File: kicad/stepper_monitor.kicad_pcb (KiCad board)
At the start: 2 copper layers, 44 x 48 mm, 89 parts, among them J1 Conn_01x02_Pin, J2 Conn_01x04_Pin, J3 USB_C_Receptacle_USB2.0, J4 Conn_01x04_Pin, J5 Conn_01x04_Pin, J6 JTAG, Q1 MMDT2222A, SW1 SW_Push, U1 5V, U2 AMS1117-3.3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

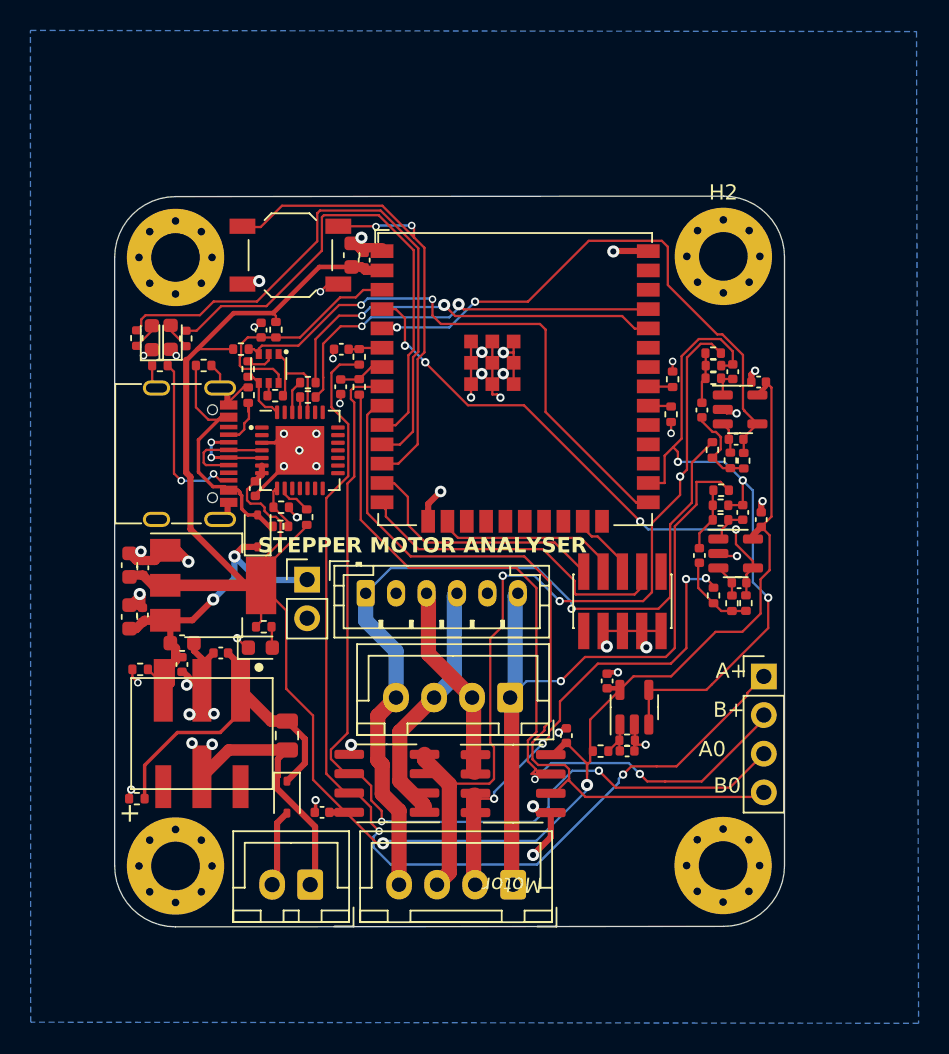
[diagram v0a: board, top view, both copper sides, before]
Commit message: Used ESP32 with Integrated antenna
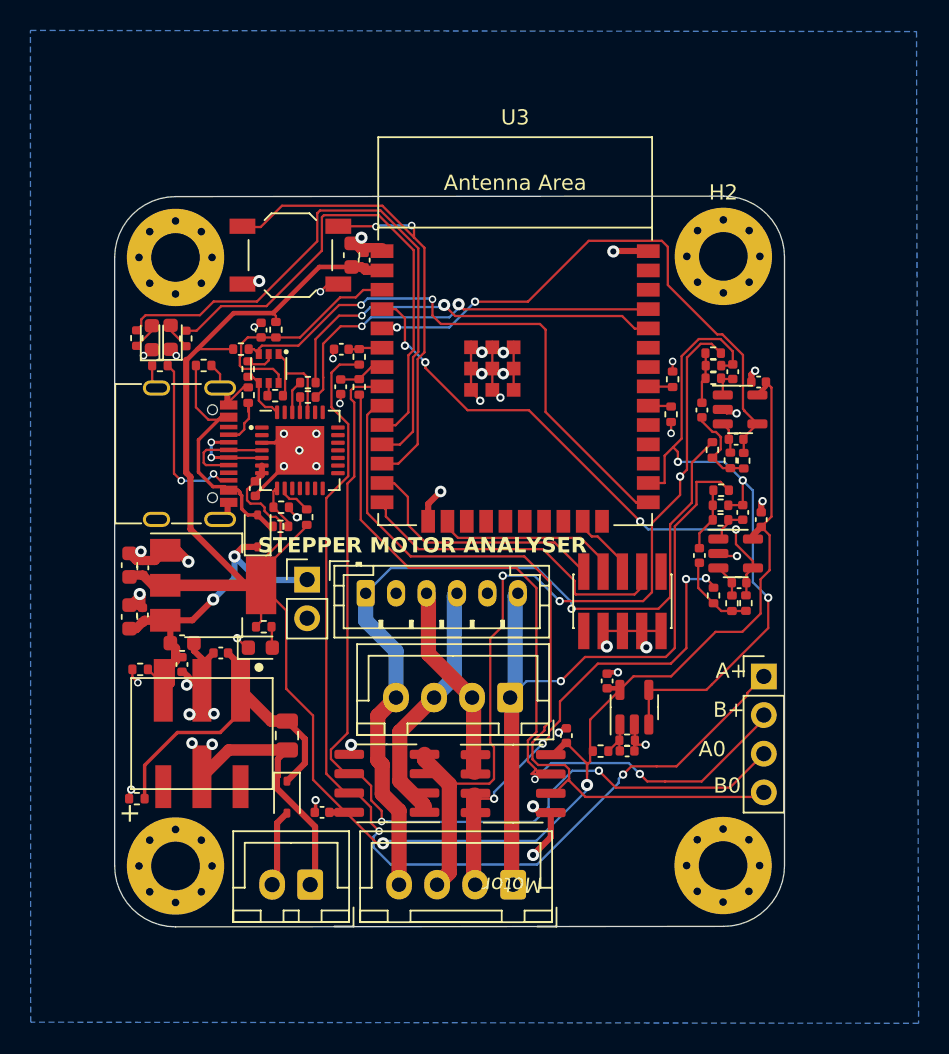
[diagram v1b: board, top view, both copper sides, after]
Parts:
- U3: footprint stepper_monitor:ESP32-WROOM-32UE -> stepper_monitor:ESP32-WROOM-32E

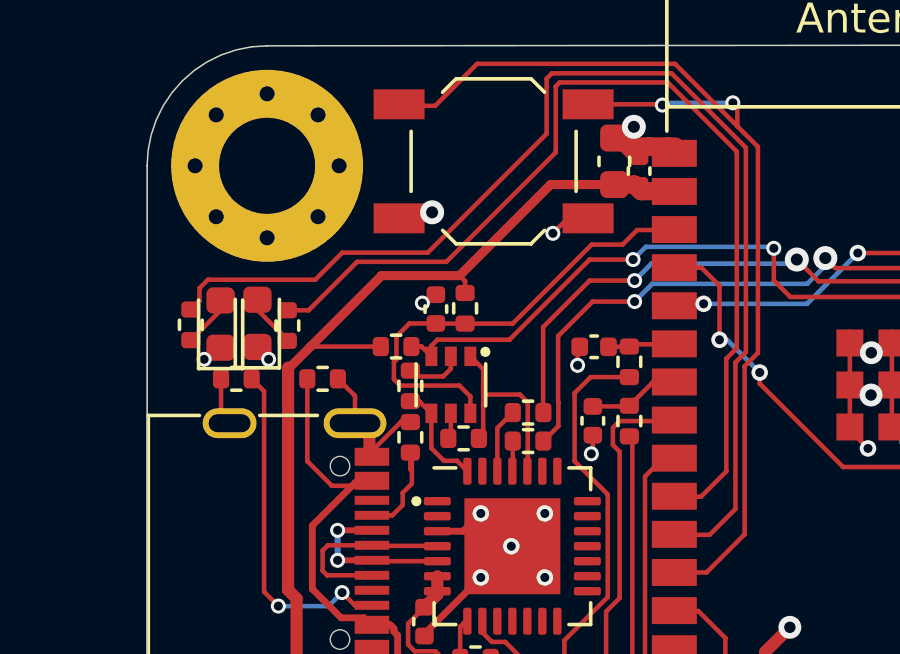
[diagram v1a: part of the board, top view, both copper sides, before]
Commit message: Replaced Extended part transistors with basic mosfets
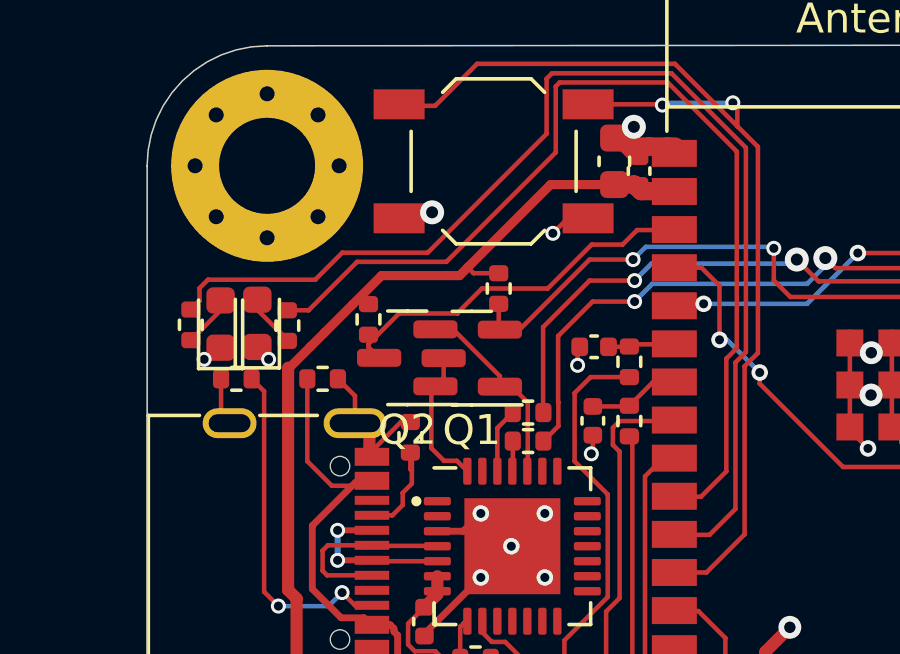
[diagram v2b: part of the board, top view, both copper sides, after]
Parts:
- removed C26: 2u2, Capacitor_SMD:C_0402_1005Metric
- removed R30, R34: 5K1, Resistor_SMD:R_0402_1005Metric
- added Q2: 2N7002, Package_TO_SOT_SMD:SOT-23, F.Cu at (8.67, -34.1)
- Q1: value MMDT2222A -> 2N7002; footprint stepper_monitor:SOT-363_SC-70-6 -> Package_TO_SOT_SMD:SOT-23
- moved R35 3.93 mm to (11.7, -36.4), turned to 90 degrees
- moved R29 3.24 mm to (7.38, -35.4)
- moved Q1 1.13 mm to (10.8, -34.1)
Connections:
- Q1 pad 2: Net-(Q1A-B1) -> IO0
- Q1 pad 3: IO0 -> DTR
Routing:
- net EN: track 15.8 -> 12.7 mm
- net IO0: track 37.5 -> 34.7 mm
- net Net-(Q1A-B1): track 1.95 -> 0.00 mm
- net +3V3: track 143.9 -> 142.0 mm
- net DTR: track 3.55 -> 4.69 mm
- net Net-(Q1B-B2): track 0.87 -> 0.00 mm
- net RTS: track 7.29 -> 6.68 mm
- net GNDD: track 106.9 -> 106.3 mm, vias 48 -> 47

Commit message: Added 5pin uart programming header. Fixed led resistor part number.  Normal switching reverse polarity diode
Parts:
- D2: value 1N5819WS -> 1N4148WS
- R31, R32, R33: value 5K1 -> 2k
- TP1: footprint Connector_PinHeader_2.54mm:PinHeader_1x02_P2.54mm_Vertical -> Connector_PinHeader_2.54mm:PinHeader_1x05_P2.54mm_Vertical
- moved D5 7.86 mm to (1.72, -14.8)
- moved C3 4.88 mm to (10.6, -4.24), turned to 180 degrees
- moved D2 1.44 mm to (12.0, -6.30), turned to 0 degrees
- moved C14 0.27 mm to (13.4, -3.98)
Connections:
- TP1 pad 1: +5V -> +3V3
- TP1 pad 2: GNDD -> +5V
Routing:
- net TXD0: track 26.5 -> 49.3 mm, vias 2 -> 4
- net RXD0: track 26.3 -> 46.1 mm, vias 2 -> 4
- net GNDD: track 106.3 -> 96.9 mm, vias 47 -> 46
- net Net-(D5-A): track 1.69 -> 10.3 mm, vias 0 -> 2
- net Net-(D2-A): track 5.10 -> 8.71 mm
- net +3V3: track 142.0 -> 145.5 mm
- net +12V: track 23.0 -> 25.2 mm
- net +5V: track 26.7 -> 27.3 mm
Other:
- board text added: "3 5 Rx Tx G"
- board text added: "3.3"
